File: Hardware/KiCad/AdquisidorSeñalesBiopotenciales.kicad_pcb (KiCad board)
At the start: 2 copper layers, 87.6 x 97 mm, 59 parts, among them J1 Entradas Analógicas, P1_17 Conn_01x01_Socket, P1_23 Conn_01x01_Socket, P1_25 Conn_01x01_Socket, P1_27 Conn_01x01_Socket, P1_29 Conn_01x01_Socket, P1_31 Conn_01x01_Socket, P1_33 Conn_01x01_Socket, P1_7 Conn_01x01_Socket, P2_1 Conn_01x01_Socket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

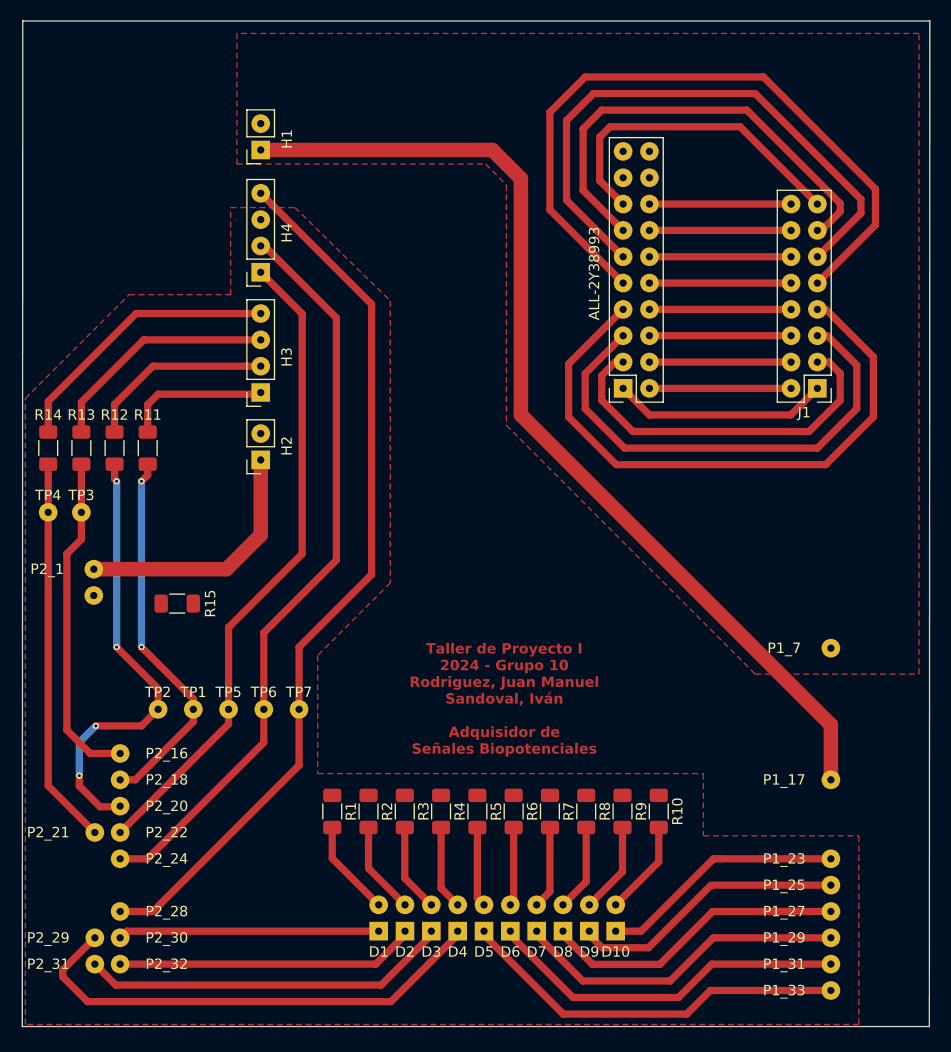
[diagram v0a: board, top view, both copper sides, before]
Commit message: Correccion archivos KiCad
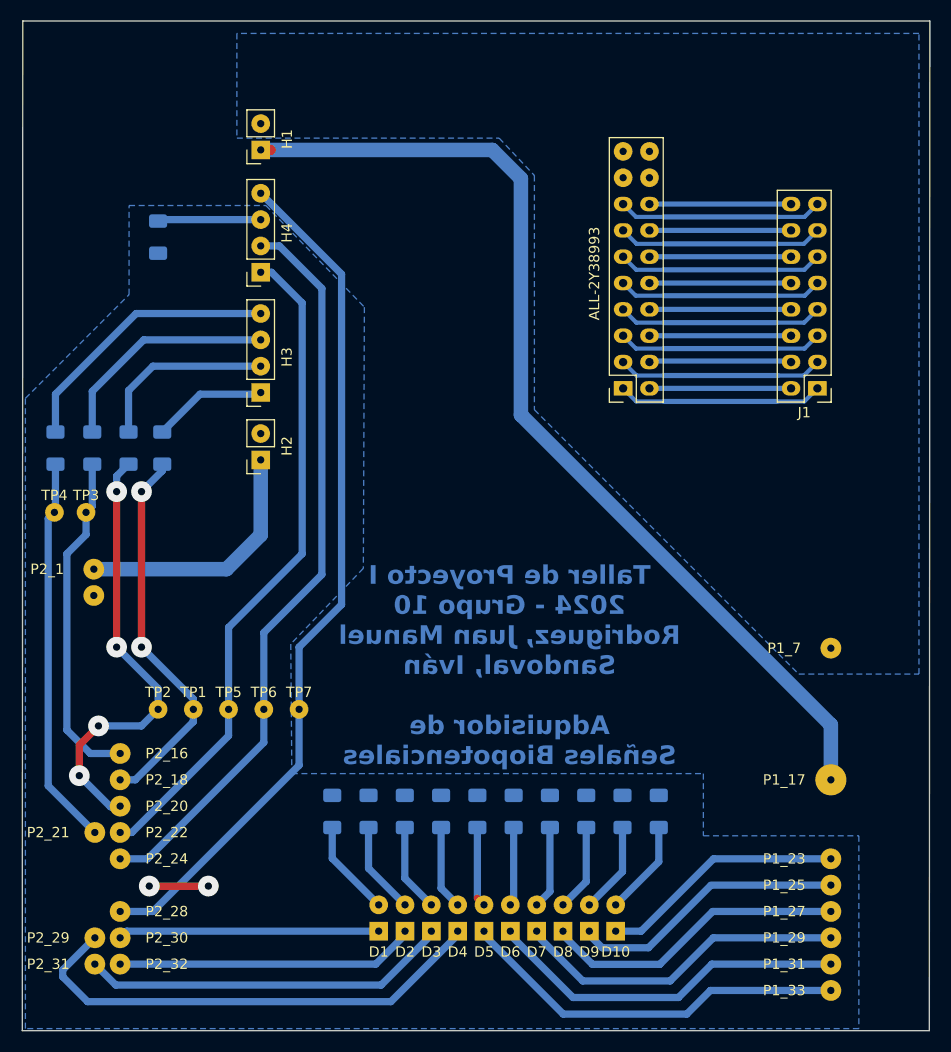
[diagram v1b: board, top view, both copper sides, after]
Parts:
- R1, R10, R11, R12, R13, R14, R15, R2, R3, R4, R5, R6, R7, R8, R9: moved to B.Cu
- moved R15 35.4 mm to (75.6, 62.5), turned to 90 degrees
- moved R11 1.40 mm to (76.0, 82.8)
- moved R12 1.35 mm to (72.8, 82.8)
- moved R13 1.05 mm to (69.2, 82.8)
- moved R14 0.70 mm to (65.7, 82.8)
- moved TP4 0.60 mm to (65.6, 89.0)
- moved TP3 0.45 mm to (68.7, 89.0)
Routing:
- net Net-(ALL-2Y38993-Pin_9): track 68.1 -> 19.8 mm
- net Net-(ALL-2Y38993-Pin_7): track 58.9 -> 19.8 mm
- net Net-(ALL-2Y38993-Pin_11): track 56.4 -> 19.8 mm
- net Net-(ALL-2Y38993-Pin_5): track 47.1 -> 19.8 mm
- net Net-(ALL-2Y38993-Pin_13): track 44.4 -> 19.8 mm
- net Net-(ALL-2Y38993-Pin_3): track 35.7 -> 19.8 mm
- net Net-(ALL-2Y38993-Pin_15): track 31.9 -> 19.8 mm
- net Net-(H4-Pin_3): track 0.00 -> 9.96 mm
- net GND: track 0.00 -> 5.70 mm, vias 0 -> 2
- net Net-(H3-Pin_1): track 14.0 -> 11.1 mm
- net LCD2: track 85.6 -> 83.2 mm
- net LCD4: track 63.3 -> 64.6 mm
- net Net-(ALL-2Y38993-Pin_1): track 20.9 -> 19.8 mm
- net SPI_MISO: track 36.5 -> 37.2 mm
- net Net-(H3-Pin_2): track 18.3 -> 17.7 mm
- added copper zone on B.Cu, net GND
- added copper zone on B.Cu, net GNDA
- removed copper zone on F.Cu, net GND
- removed copper zone on F.Cu, net GNDA
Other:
- board size 87.6 x 97 mm -> 87.6 x 97.4 mm
